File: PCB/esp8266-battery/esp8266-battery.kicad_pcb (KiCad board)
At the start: 2 copper layers, 29 x 22 mm, 29 parts, among them J1 2xAA, J2 program, J3 BME280 modul, P1 ICT-Point, P2 ICT-Point, P3 ICT-Point, P4 ICT-Point, SW1 reset, SW2 boot, U1 ESP-07

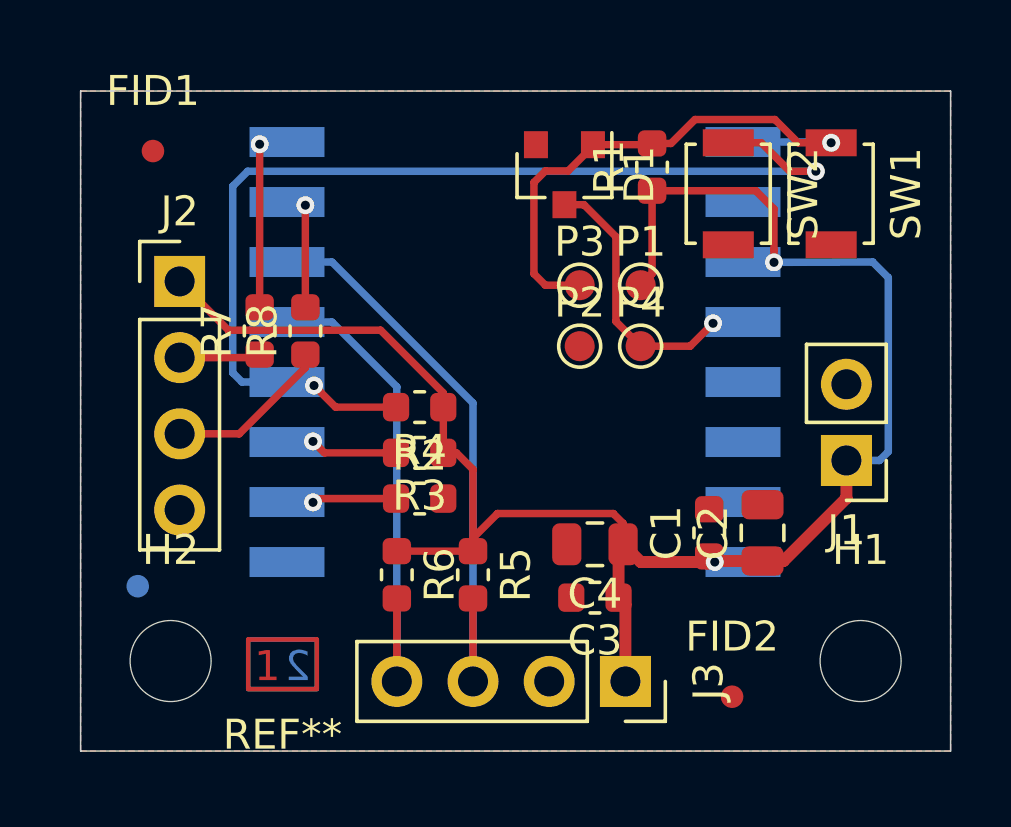
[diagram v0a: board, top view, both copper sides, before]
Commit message: Change the debug connector to TC2030-6
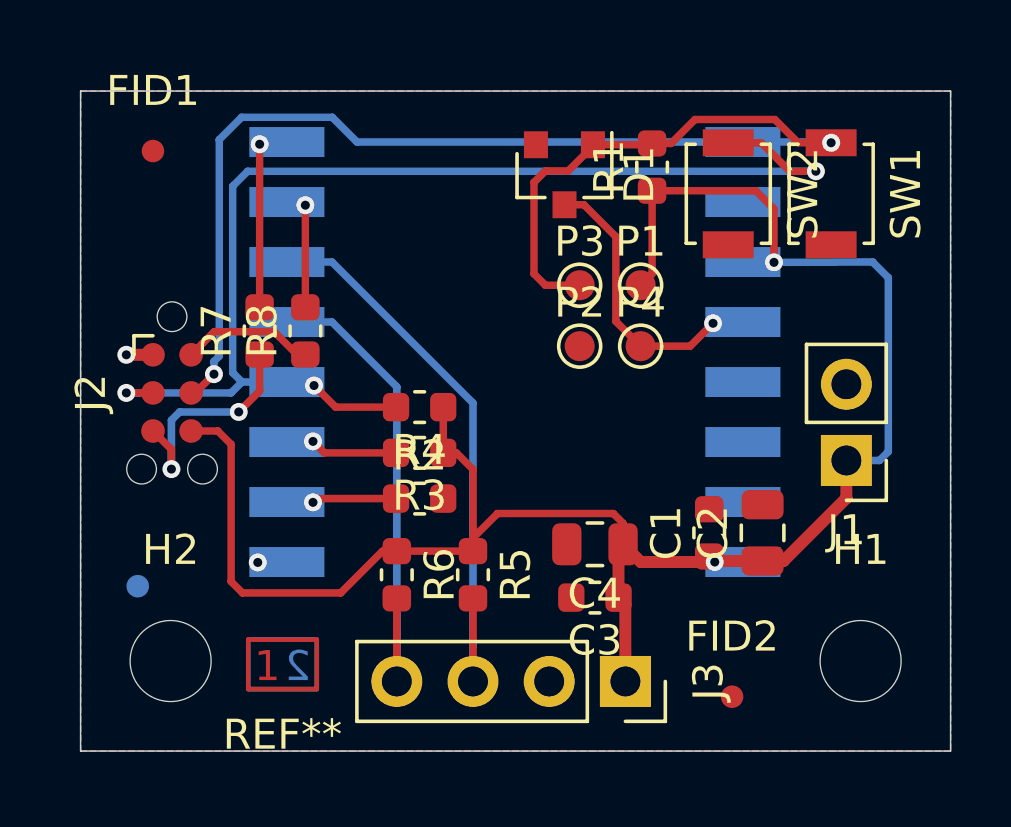
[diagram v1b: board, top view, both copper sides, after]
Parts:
- J2: footprint Connector_PinHeader_2.54mm:PinHeader_1x04_P2.54mm_Vertical -> Connector:Tag-Connect_TC2030-IDC-NL_2x03_P1.27mm_Vertical
- moved J2 3.73 mm to (122.0, 97.1), turned to 270 degrees
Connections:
- J2 pad 1: +3V3 -> GND
- J2 pad 2: /RXD -> /TXD
- J2 pad 3: /TXD -> /IO0
- J2 pad 4: GND -> /~RST
- U1 pad 2: (no net) -> Net-(U1-Pad2)
- U1 pad 5: (no net) -> Net-(U1-Pad5)
- U1 pad 6: (no net) -> Net-(U1-Pad6)
- U1 pad 7: (no net) -> Net-(U1-Pad7)
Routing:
- net /~RST: track 18.8 -> 45.9 mm, vias 1 -> 2
- net /RXD: track 2.71 -> 7.73 mm, vias 0 -> 2
- net /IO0: track 35.1 -> 40.0 mm, vias 2 -> 3
- net +3V3: track 64.2 -> 65.8 mm
- net /TXD: track 5.54 -> 4.44 mm
- net GND: track 0.00 -> 0.89 mm, vias 0 -> 2
